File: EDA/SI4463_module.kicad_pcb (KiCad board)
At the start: 4 copper layers, 51.4 x 21 mm, 45 parts, among them J1 EXT_ANT, J2 Conn_01x10_Pin, J3 U. FL, U1 SI4463-C2A-GMR, U2 SKY66423-11, Y1 30MHz

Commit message: Finished PCB
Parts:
- moved TR1 12.2 mm to (108.4, 80.8), turned to 0 degrees
- moved R4 5.04 mm to (107.4, 84.5), turned to 90 degrees
- moved J2 4.52 mm to (104.9, 75.5)
- moved D1 3.67 mm to (107.4, 88.5), turned to -90 degrees
- moved C9 3.21 mm to (107.2, 92.6)
- moved Y1 0.29 mm to (123.6, 89.3)
- moved R5 0.27 mm to (111.0, 91.4), turned to 0 degrees
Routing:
- net /EN: track 4.02 -> 18.0 mm, vias 0 -> 2
- net /CSD: track 26.3 -> 38.6 mm
- net /CPS: track 43.4 -> 37.9 mm
- net /SPI_SDI: track 17.0 -> 12.4 mm
- net /SPI_CSn: track 16.4 -> 11.9 mm
- net /SPI_CLK: track 18.1 -> 13.6 mm
- net /INTn: track 18.8 -> 14.2 mm
- net /SPI_SDO: track 17.5 -> 13.0 mm
- net Net-(R4-Pad2): track 3.15 -> 0.00 mm
- net Net-(D1-PadK): track 2.69 -> 0.00 mm
- net VCC: track 19.0 -> 21.1 mm, vias 6 -> 10
- net /CTX: track 24.0 -> 24.8 mm
- net /LNA: track 0.00 -> 0.50 mm
- net GND: vias 0 -> 400
- added copper zone on B.Cu, net GND
- added copper zone on F.Cu, net GND
- added copper zone on In1.Cu, net GND
- added copper zone on F.Cu, net VCC
- added copper zone on In2.Cu, net VCC
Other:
- board size 51.4 x 21 mm -> 46.9 x 21 mm

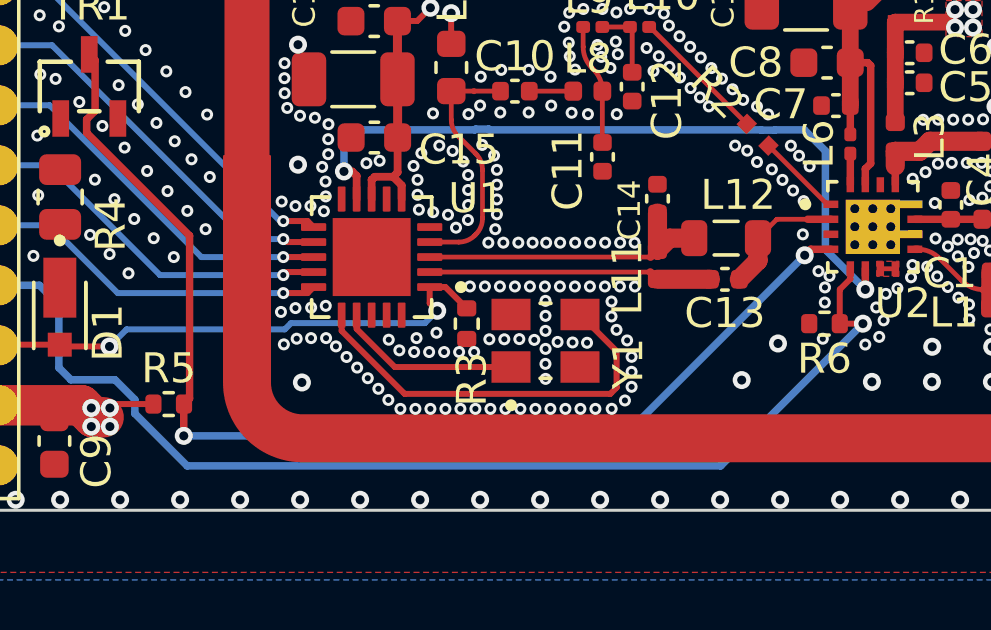
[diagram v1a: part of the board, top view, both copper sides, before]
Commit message: Forgot to add stitching on RX differential input section.
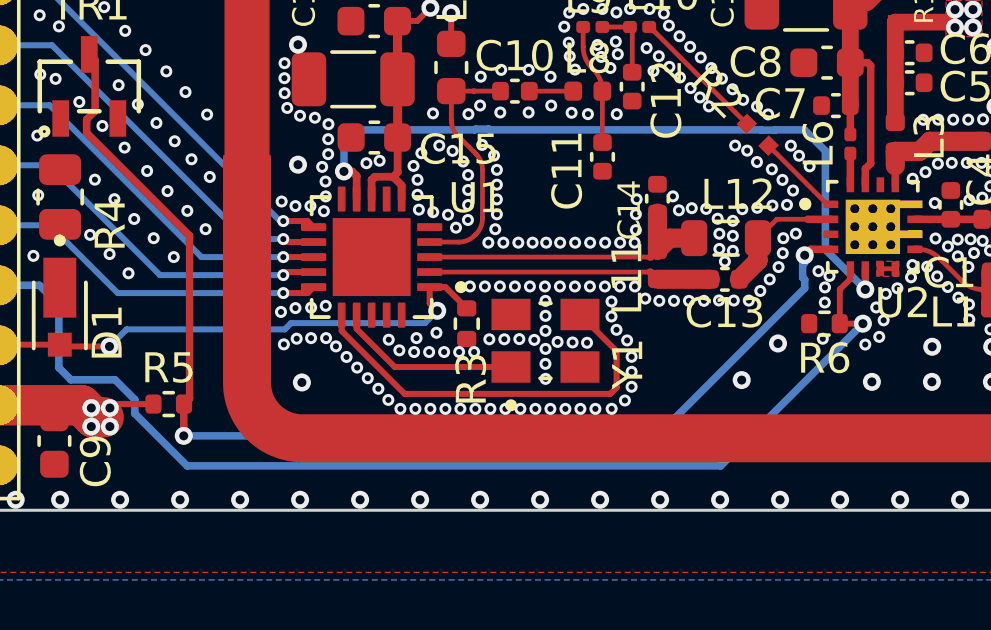
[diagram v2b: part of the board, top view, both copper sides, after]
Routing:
- net /CSD: track 38.6 -> 39.3 mm
- net GND: vias 400 -> 431

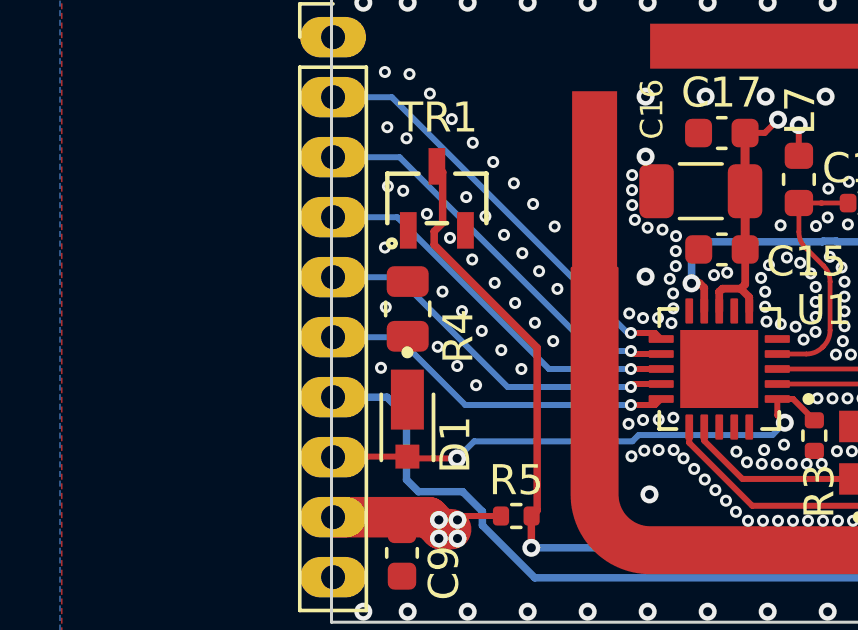
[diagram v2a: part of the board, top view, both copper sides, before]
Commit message: added 2 missing traces
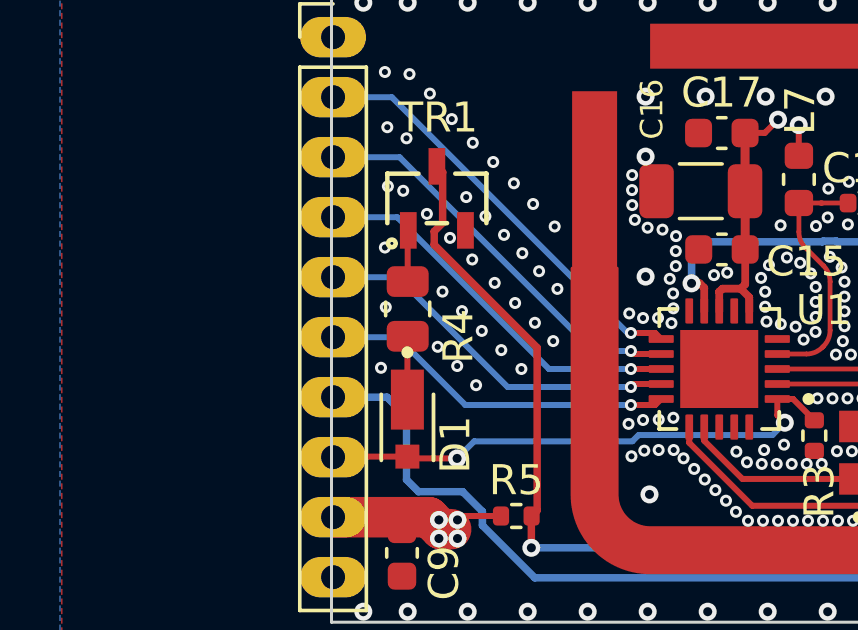
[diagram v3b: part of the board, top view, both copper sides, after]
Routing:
- net Net-(D1-PadK): track 0.00 -> 2.11 mm
- net Net-(R4-Pad2): track 0.00 -> 1.71 mm
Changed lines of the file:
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@@
+	)
+	(segment
+		(start 107.4 87.53)
+		(end 107.4 85.43)
+		(width 0.2)
+		(layer "F.Cu")
+		(net 16)
+	)
+	(segment
+		(start 107.4 85.43)
+		(end 107.41 85.42)
+		(width 0.2)
+		(layer "F.Cu")
+		(net 16)
 	)
 	(segment
@@
 	)
 	(segment
+		(start 107.41 81.91)
+		(end 107.43 81.89)
+		(width 0.2)
+		(layer "F.Cu")
+		(net 27)
+	)
+	(segment
+		(start 107.41 83.595)
+		(end 107.41 81.91)
+		(width 0.2)
+		(layer "F.Cu")
+		(net 27)
+	)
+	(segment
